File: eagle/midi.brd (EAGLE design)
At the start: 62.5 x 83.8 mm, 62 parts, among them CON2 EXPANSION-PORT, IC1 SST39VF1681, IC12 74LS14, IC16 74LVC8T245, IC18 MCP1703CB, IC2 XC9572XL_TQ100, IC3 6N138SMD, IC4 12MHz, IC5 CY61228EV30

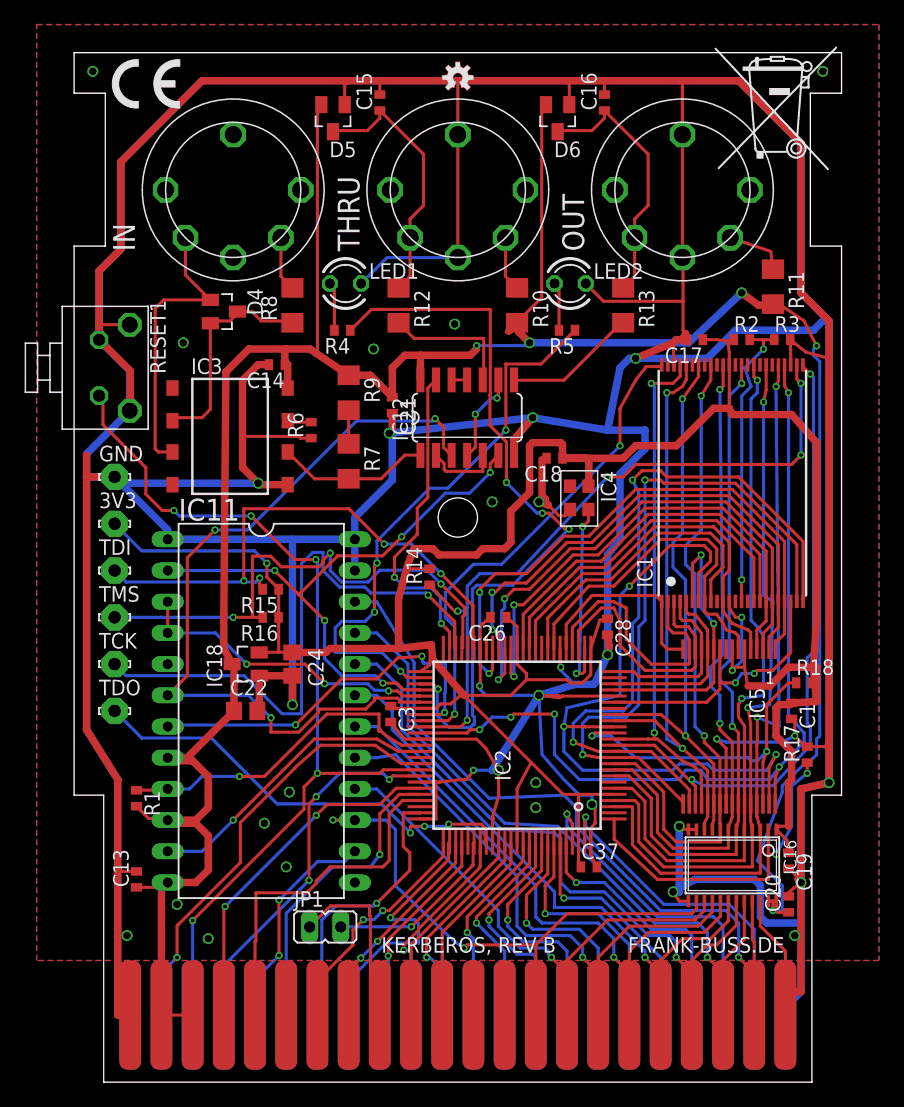
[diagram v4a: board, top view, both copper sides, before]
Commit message: new 4 layer board
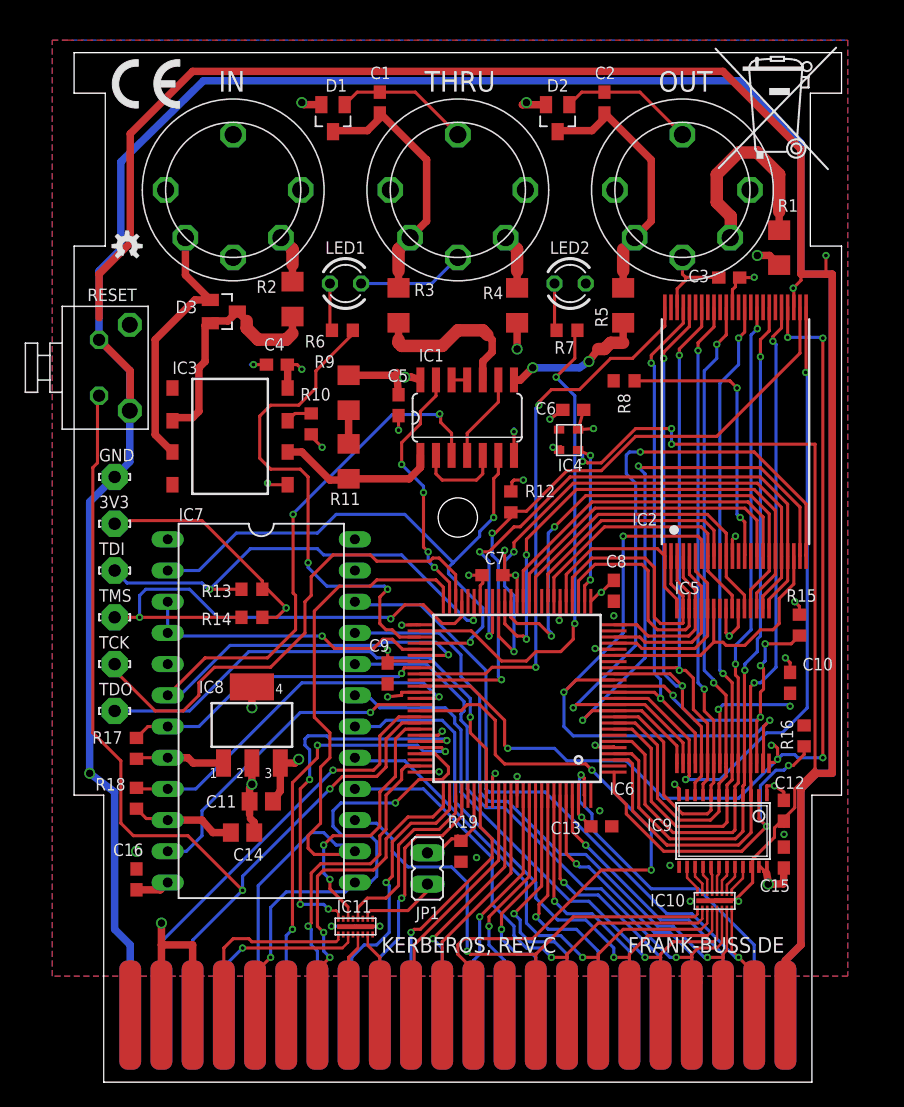
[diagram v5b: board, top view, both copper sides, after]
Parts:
- removed C17, C18, C19, C20, C21, C26, C28, C37: 100n, rcl:C0402
- removed C22: 10u, rcl:C0805
- removed C24: 1u, rcl:C0805
- removed IC12: 74LS14, 74xx-eu:SO14
- removed IC16: 74LVC8T245, 74lvc8t245:TSSOP24
- removed IC18: MCP1703CB, linear:SOT23
- added C10, C12, C4, C5, C6, C7, C8, C9: 100n, rcl:C0603
- added C11: 1u, rcl:C0805
- added C2: 1n, rcl:C0603
- added IC10: EMI-FILTER, emv-filter:HUSON16
- added IC6: XC95144XL_TQ100, xc9572xl-tq100:TQ100
- added IC7: (no value), micro-motorola:DIL24
- added IC8: MCP1703DB, mcp1703:SOT223
- added IC9: 74LVC8T245, 74lvc8t245:TSSOP24
- added R19: 10k, rcl:R0603
- C1: value 100n -> 1n; device rcl:C0402 -> rcl:C0603
- C13, C3: device rcl:C0402 -> rcl:C0603
- C14: value 100n -> 10u; device rcl:C0402 -> rcl:C0805
- C15, C16: value 1n -> 100n; device rcl:C0402 -> rcl:C0603
- IC1: value SST39VF1681 -> 74LS14; device flash:TSOP48 -> 74xx-eu:SO14
- IC11: value (none) -> EMI-FILTER; device micro-motorola:DIL24 -> emv-filter:HUSON16
- IC2: value XC9572XL_TQ100 -> SST39VF1681; device xc9572xl-tq100:TQ100 -> flash:TSOP48
- IC4: value 12MHz -> 48MHz
- R1, R2, R3: value 10k -> 220; device rcl:R0402 -> rcl:R1206
- R10, R12, R8: value 220 -> 10k; device rcl:R1206 -> rcl:R0603
- R13: value 220 -> 4k7; device rcl:R1206 -> rcl:R0603
- R14, R17: value 10k -> 4k7; device rcl:R0402 -> rcl:R0603
- R15, R16: value 4k7 -> 10k; device rcl:R0402 -> rcl:R0603
- R18: device rcl:R0402 -> rcl:R0603
- R4, R5: value 1k -> 220; device rcl:R0402 -> rcl:R1206
- R6: value 10k -> 1k; device rcl:R0402 -> rcl:R0603
- R7: value 220 -> 1k; device rcl:R1206 -> rcl:R0603
- U$1: device logo:MUELLTONNE_10.00 -> logo:CE-4MM
- U$2: device logo:CE-4MM -> logo:MUELLTONNE_10.00
- moved C16 73.8 mm to (3.05, 16.8)
- moved C15 69.7 mm to (55.8, 18.5)
- moved R1 68.9 mm to (55.4, 68.2)
- moved C1 59.8 mm to (22.9, 80.0), turned to 90 degrees
- moved R18 55.2 mm to (3.05, 23.4), turned to 270 degrees
- moved R17 54.6 mm to (3.05, 27.4), turned to 270 degrees
- moved U$1 48.8 mm to (1.02, 79.5)
- moved U$2 48.8 mm to (49.5, 74.2)
- moved C3 45.0 mm to (51.3, 65.8), turned to 180 degrees
- moved R16 44.5 mm to (57.4, 28.4), turned to 90 degrees
- moved R15 43.2 mm to (57.0, 37.5), turned to 90 degrees
- moved C14 38.2 mm to (11.7, 20.6), turned to 0 degrees
- moved C13 38.1 mm to (40.9, 21.1), turned to 0 degrees
- moved R13 38.1 mm to (12.4, 40.4), turned to 180 degrees
- moved R11 37.4 mm to (20.3, 50.8)
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- renumbered CON2 to CON1, D4 to D3, D5 to D1, D6 to D2, RESET1 to RESET
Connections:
- new net EXROM-F: IC11.10, JP1.1
- new net GAME-F: IC11.12, IC6.78
- new net IRQ-F: IC11.16, IC6.70
- new net N$10: IC10.6, IC9.16
- new net N$11: IC10.5, IC9.17
- new net N$12: IC10.4, IC9.18
- new net N$14: IC10.3, IC9.19
- new net N$15: IC10.2, IC9.20
- new net N$16: IC10.1, IC9.21
- new net N$8: IC10.8, IC9.14
- new net N$9: IC10.7, IC9.15
- new net NMI-F: IC11.14, IC6.68
- net +3V3: now also C10.1, C11.1, C12.1, C13.1, C6.1, C7.1, C8.1, C9.1, IC2.12, IC2.37, IC6.26, IC6.38, IC6.5, IC6.51, IC6.57, IC6.88, IC6.98, IC8.3, IC9.1, R12.2, R13.1, R14.1, R15.2; no longer C1.1, C17.1, C18.1, C19.1, C24.1, C26.1, C28.1, C37.1, IC1.12, IC1.37, IC16.1, IC18.2, IC2.26, IC2.38, IC2.5, IC2.51, IC2.57, IC2.88, IC2.98, R14.2, R15.1, R16.1, R18.2, R2.1
- net +5V: now also C15.1, C16.1, C4.1, C5.1, IC1.14, IC7.10, IC7.12, IC7.8, IC8.1, IC9.23, IC9.24, R17.2, R18.2, R4.2; no longer C13.1, C20.1, C21.1, C22.1, IC11.10, IC11.12, IC11.8, IC12.14, IC16.23, IC16.24, IC18.3, R10.2, R11.2
- net 6850-CS2: now also IC6.63, IC7.9, R18.1; no longer IC11.9, IC2.63, R1.1
- net 6850-IRQ: now also IC6.58, IC7.7, R17.1; no longer IC11.7, IC2.58
- net 6850-RS: now also IC6.64, IC7.11; no longer IC11.11, IC2.64
- net 6850-RX/TX-CLK: now also IC6.55, IC7.3, IC7.4; no longer IC11.3, IC11.4, IC2.55
- net 6850-RXDATA: now also IC1.6, IC6.54, IC7.2; no longer IC11.2, IC12.6, IC2.54
- net 6850-TXDATA: now also IC1.3, IC6.56, IC7.6; no longer IC11.6, IC12.3, IC2.56
- net A0: now also IC6.99; no longer IC2.99
- net A1: now also IC6.97; no longer IC2.97
- net A10: now also IC6.86; no longer IC2.86
- net A11: now also IC6.82; no longer IC2.82
- net A12: now also IC6.79; no longer IC2.79
- net A13: now also IC6.77; no longer IC2.77
- net A14: now also IC6.74; no longer IC2.74
- net A15: now also IC6.71; no longer IC2.71
- net A2: now also IC6.96; no longer IC2.96
- net A3: now also IC6.95; no longer IC2.95
- net A4: now also IC6.94; no longer IC2.94
- net A5: now also IC6.93; no longer IC2.93
- net A6: now also IC6.92; no longer IC2.92
- net A7: now also IC6.91; no longer IC2.91
- net A8: now also IC6.90; no longer IC2.90
- net A9: now also IC6.89; no longer IC2.89
- net AT0: now also IC2.45, IC6.14; no longer IC1.45, IC2.14
- net AT1: now also IC2.25, IC6.13; no longer IC1.25, IC2.13
- net AT10: now also IC2.7, IC6.16; no longer IC1.7, IC2.16
- net AT11: now also IC2.6, IC6.22; no longer IC1.6, IC2.22
- net AT12: now also IC2.5, IC6.23; no longer IC1.5, IC2.23
- net AT13: now also IC2.4, IC6.25; no longer IC1.4, IC2.25
- net AT14: now also IC2.3, IC6.28; no longer IC1.3, IC2.28
- net AT15: now also IC2.2, IC6.29; no longer IC1.2, IC2.29
- net AT16: now also IC2.1, IC6.30; no longer IC1.1, IC2.30
- net AT17: now also IC2.48, IC6.59; no longer IC1.48, IC2.59
- net AT18: now also IC2.17, IC6.37; no longer IC1.17, IC2.37
- net AT19: now also IC2.16, IC6.36; no longer IC1.16, IC2.36
- net AT2: now also IC2.24, IC6.12; no longer IC1.24, IC2.12
- net AT20: now also IC2.9, IC6.33; no longer IC1.9, IC2.33
- net AT3: now also IC2.23, IC6.11; no longer IC1.23, IC2.11
- net AT4: now also IC2.22, IC6.20; no longer IC1.22, IC2.20
- net AT5: now also IC2.21, IC6.42; no longer IC1.21, IC2.42
- net AT6: now also IC2.20, IC6.41; no longer IC1.20, IC2.41
- net AT7: now also IC2.19, IC6.40; no longer IC1.19, IC2.40
- net AT8: now also IC2.18, IC6.39; no longer IC1.18, IC2.39
- net AT9: now also IC2.8, IC6.32; no longer IC1.8, IC2.32
- net BA: now also IC6.65; no longer IC2.65
- net D0: now also IC10.16, IC7.22; no longer IC11.22, IC16.21
- net D1: now also IC10.15, IC7.21; no longer IC11.21, IC16.20
- net D2: now also IC10.14, IC7.20; no longer IC11.20, IC16.19
- net D3: now also IC10.13, IC7.19; no longer IC11.19, IC16.18
- net D4: now also IC10.12, IC7.18; no longer IC11.18, IC16.17
- net D5: now also IC10.11, IC7.17; no longer IC11.17, IC16.16
- net D6: now also IC10.10, IC7.16; no longer IC11.16, IC16.15
- net D7: now also IC10.9, IC7.15; no longer IC11.15, IC16.14
- net DIR: now also IC6.1, IC9.2, R16.1; no longer IC16.2, IC2.1, R17.1
- net DT0: now also IC2.29, IC6.3, IC9.3; no longer IC1.29, IC16.3, IC2.3
- net DT1: now also IC2.31, IC6.4, IC9.4; no longer IC1.31, IC16.4, IC2.4
- net DT2: now also IC2.33, IC6.6, IC9.5; no longer IC1.33, IC16.5, IC2.6
- net DT3: now also IC2.35, IC6.8, IC9.6; no longer IC1.35, IC16.6, IC2.8
- net DT4: now also IC2.38, IC6.9, IC9.7; no longer IC1.38, IC16.7, IC2.9
- net DT5: now also IC2.40, IC6.10, IC9.8; no longer IC1.40, IC16.8, IC2.10
- net DT6: now also IC2.42, IC6.18, IC9.9; no longer IC1.42, IC16.9, IC2.18
- net DT7: now also IC2.44, IC6.17, IC9.10; no longer IC1.44, IC16.10, IC2.17
- net EXROM: now also IC11.7; no longer JP1.1
- net FLASH-CE: now also IC2.26, IC6.60, R12.1; no longer IC1.26, IC2.60, R14.1
- net GAME: now also IC11.5; no longer IC2.78
- net GND: now also C10.2, C11.2, C12.2, C2.2, C4.2, C5.2, C6.2, C7.2, C8.2, C9.2, IC1.7, IC10.GND, IC11.GND, IC2.27, IC2.46, IC6.100, IC6.21, IC6.31, IC6.44, IC6.62, IC6.69, IC6.75, IC6.84, IC7.1, IC7.23, IC7.24, IC8.2, IC8.4, IC9.11, IC9.12, IC9.13, IC9.22, R10.1, R16.2, R19.2, R8.2; no longer C17.2, C18.2, C19.2, C20.2, C21.2, C22.2, C24.2, C26.2, C28.2, C37.2, IC1.27, IC1.46, IC11.1, IC11.23, IC11.24, IC12.7, IC16.11, IC16.12, IC16.13, IC16.22, IC18.1, IC2.100, IC2.21, IC2.31, IC2.44, IC2.62, IC2.69, IC2.75, IC2.84, R17.2, R3.2, R6.1
- net IO1: now also IC6.76; no longer IC2.76
- net IO2: now also IC6.85; no longer IC2.85
- net IRQ: now also IC11.1; no longer IC2.70
- net LED1: now also IC6.53, R6.1; no longer IC2.53, R4.1
- net LED2: now also IC6.52, R7.1; no longer IC2.52, R5.1
- net MIDI-OUT-INVERTED: now also IC1.4, IC1.9; no longer IC12.4, IC12.9
- net MIDI-THRU: now also IC1.13, IC6.49; no longer IC12.13, IC2.49
- net N$1: now also R10.2; no longer R6.2
- net N$13: now also IC2.14, R8.1; no longer IC1.14, R2.2, R3.1
- net N$18: now also R7.2; no longer R5.2
- net N$2: now also IC6.27; no longer IC2.27
- net N$3: now also R11.1; no longer R7.1
- net N$38: now also R2.2; no longer R8.2
- net N$39: now also IC1.1, R11.2; no longer IC12.1, R7.2
- net N$4: now also IC1.11, IC1.12; no longer IC12.11, IC12.12
- net N$40: now also R1.1; no longer R11.1
- net N$41: now also R4.1; no longer R10.1
- net N$42: now also C2.1, R5.1; no longer C16.1, R13.1
- net N$43: now also C1.1, R3.1; no longer C15.1, R12.1
- net N$44: now also IC1.8, R5.2; no longer IC12.8, R13.2
- net N$45: now also IC1.10, R3.2; no longer IC12.10, R12.2
- net N$48: now also R2.1; no longer R8.1
- net N$5: now also IC1.2, IC1.5; no longer IC12.2, IC12.5
- net N$6: now also R6.2; no longer R4.2
- net N$7: now also IC6.81, R19.1; no longer IC2.81
- net NMI: now also IC11.3; no longer IC2.68
- net OE: now also IC2.28, IC6.61; no longer IC1.28, IC2.61
- net RAM-CE: now also IC6.15, R15.1; no longer IC2.15, R18.1
- net RESET: now also IC6.67; no longer IC2.67
- net ROMH: now also IC6.66; no longer IC2.66
- net ROML: now also IC6.87; no longer IC2.87
- net RW: now also IC6.72, IC7.13; no longer IC11.13, IC2.72
- net S02: now also IC6.50, IC7.14; no longer IC11.14, IC2.50
- net TCK: now also IC6.48; no longer IC2.48
- net TDI: now also IC6.45, R13.2; no longer IC2.45, R15.2
- net TDO: now also IC6.83; no longer IC2.83
- net TMS: now also IC6.47, R14.2; no longer IC2.47, R16.2
- net WE: now also IC2.11, IC6.35; no longer IC1.11, IC2.35
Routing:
- net GND: track 800.6 -> 526.4 mm, vias 34 -> 35
- net BA: track 0.00 -> 52.7 mm, vias 0 -> 2
- net S02: track 18.0 -> 58.6 mm, vias 2 -> 0
- net +5V: track 232.8 -> 266.7 mm, vias 5 -> 8
- net IRQ-F: track 0.00 -> 31.8 mm, vias 0 -> 4
- net +3V3: track 230.4 -> 259.2 mm, vias 3 -> 18
- net NMI-F: track 0.00 -> 22.0 mm, vias 0 -> 2
- net LED1: track 61.8 -> 41.0 mm, vias 4 -> 2
- net GAME-F: track 0.00 -> 15.4 mm
- net NMI: track 30.5 -> 15.5 mm, vias 3 -> 1
- net IRQ: track 28.8 -> 16.1 mm, vias 2 -> 0
- net N$40: track 4.94 -> 17.5 mm
- net RW: track 29.2 -> 41.6 mm, vias 0 -> 2
- net GAME: track 17.7 -> 6.88 mm, vias 2 -> 0
- net A15: track 25.2 -> 35.8 mm, vias 1 -> 3
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- added copper zone on layer 3, net +3V3
- added copper zone on layer 3, net +5V
- added copper zone on layer 2, net GND
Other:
- board text added: "KERBEROS, REV C"
- board text removed: "KERBEROS, REV B"

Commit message: new datasheets, EasyFlash starter test and cleanups
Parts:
- IC4: value 48MHz -> 24MHz
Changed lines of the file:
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@@
 <attribute name="VALUE" x="11.684" y="49.149" size="1.016" layer="27" font="vector" ratio="10" rot="R90"/>
 </element>
-<element name="IC4" library="cartridge" package="ASE" value="48MHz" x="38.354" y="52.578" smashed="yes" rot="R270">
+<element name="IC4" library="cartridge" package="ASE" value="24MHz" x="38.354" y="52.578" smashed="yes" rot="R270">
 <attribute name="OC_NEWARK" value="unknown" x="38.354" y="52.578" size="1.778" layer="27" rot="R270" display="off"/>
 <attribute name="MPN" value="" x="38.354" y="52.578" size="1.778" layer="27" rot="R270" display="off"/>

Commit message: schematic cleanup and added to documentation
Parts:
- R19, R8: value 10k -> 10k, not populated
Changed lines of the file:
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@@
 <attribute name="VALUE" x="52.316" y="47.681" size="1.016" layer="27" font="vector" ratio="10" rot="R90"/>
 </element>
-<element name="R8" library="rcl" package="R0603" value="10k" x="42.7482" y="57.3532" smashed="yes" rot="R180">
+<element name="R8" library="rcl" package="R0603" value="10k, not populated" x="42.7482" y="57.3532" smashed="yes" rot="R180">
 <attribute name="NAME" x="42.2402" y="56.3372" size="1.016" layer="25" font="vector" ratio="10" rot="R270"/>
-<attribute name="VALUE" x="43.7642" y="58.3692" size="1.016" layer="27" font="vector" ratio="10" rot="R90"/>
 </element>
 <element name="LED1" library="led" package="LED3MM" value="" x="20.066" y="65.278" smashed="yes">
@@
 <attribute name="VALUE" x="1.905" y="27.305" size="1.016" layer="27" font="vector" ratio="10" rot="R180"/>
 </element>
-<element name="R19" library="rcl" package="R0603" value="10k" x="29.464" y="19.05" smashed="yes" rot="R270">
+<element name="R19" library="rcl" package="R0603" value="10k, not populated" x="29.464" y="19.05" smashed="yes" rot="R270">
 <attribute name="NAME" x="30.861" y="21.971" size="1.016" layer="25" font="vector" ratio="10" rot="R180"/>
-<attribute name="VALUE" x="30.353" y="19.177" size="1.016" layer="27" font="vector" ratio="10"/>
 </element>
 <element name="IC8" library="mcp1703" package="SOT223" value="MCP1703DB" x="12.446" y="29.337" smashed="yes">
